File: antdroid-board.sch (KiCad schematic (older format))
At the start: 53 parts, among them Q1 BSS138, Q2 BSS138, U1 LM2678T-5.0, U2 LM2678T-5.0, U3 LM2675M-5

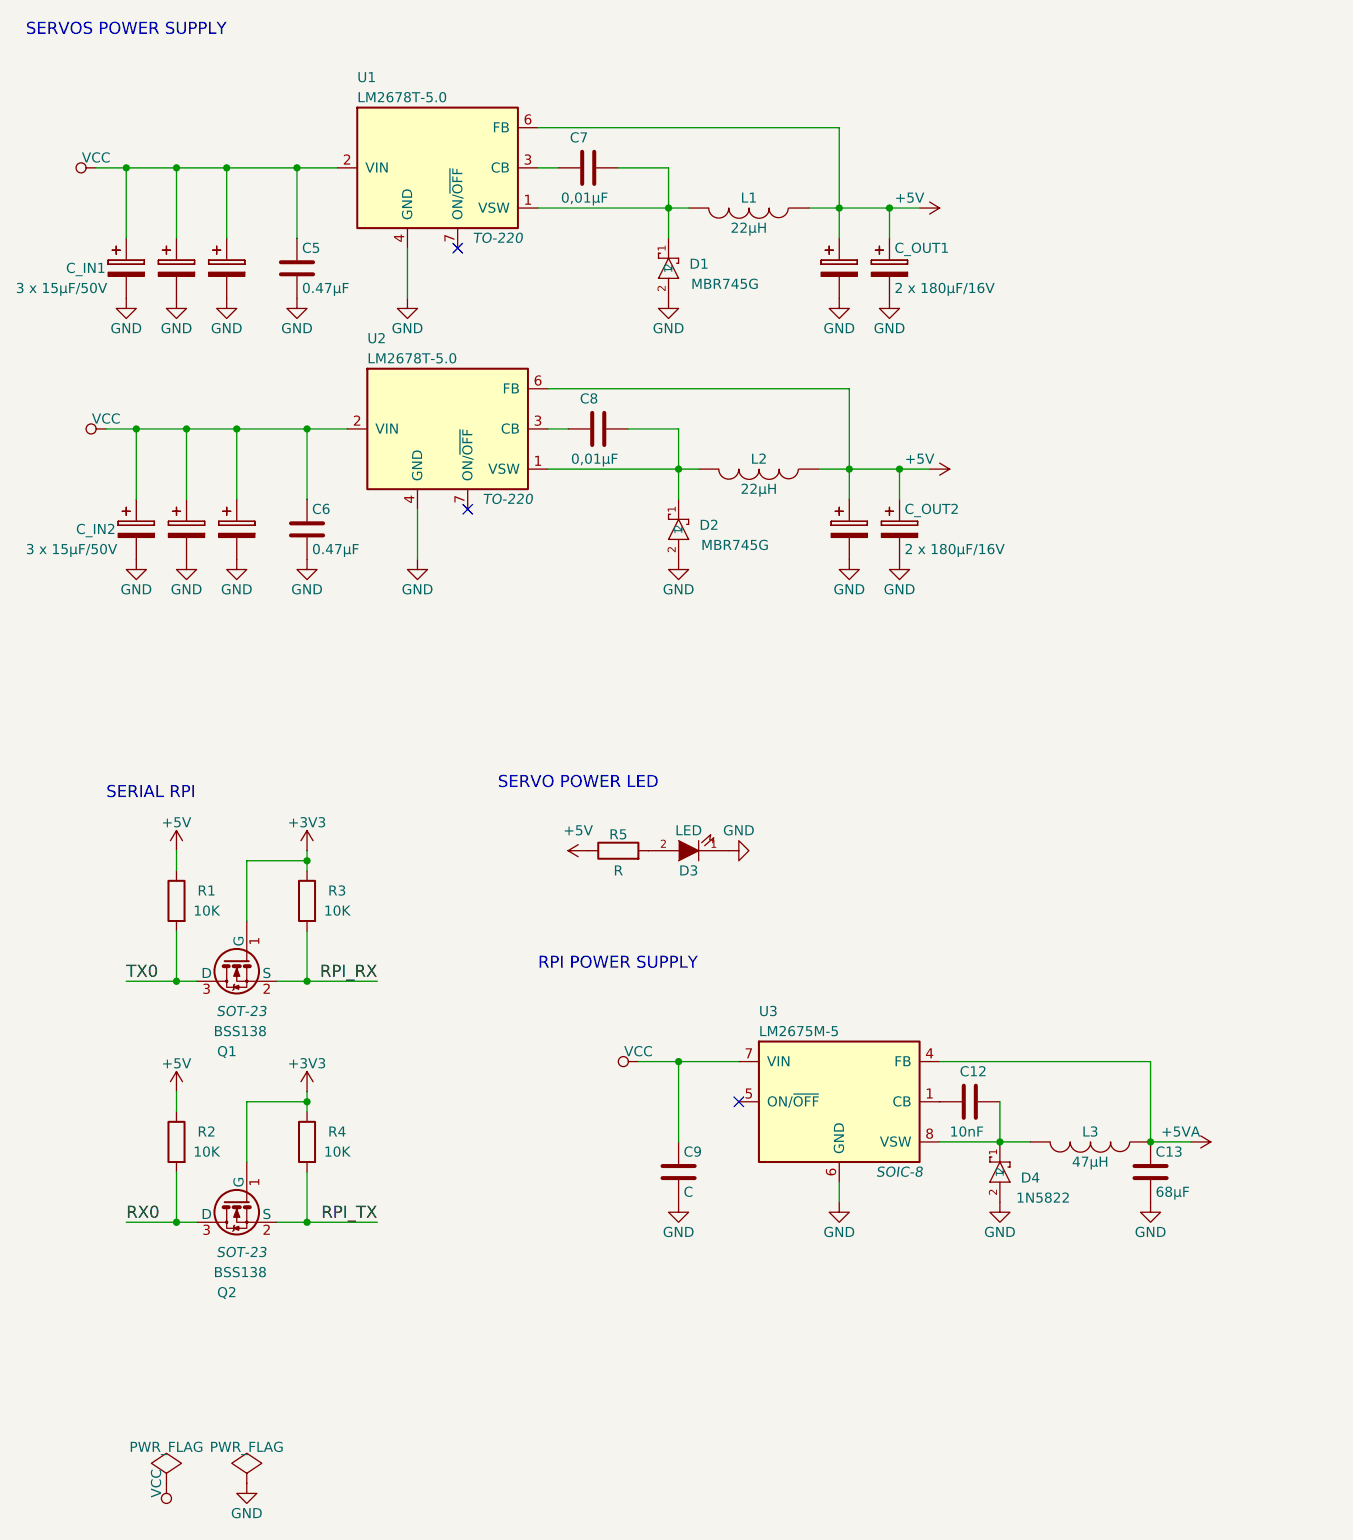
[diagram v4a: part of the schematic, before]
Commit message: PSU components fixed and some datasheet added
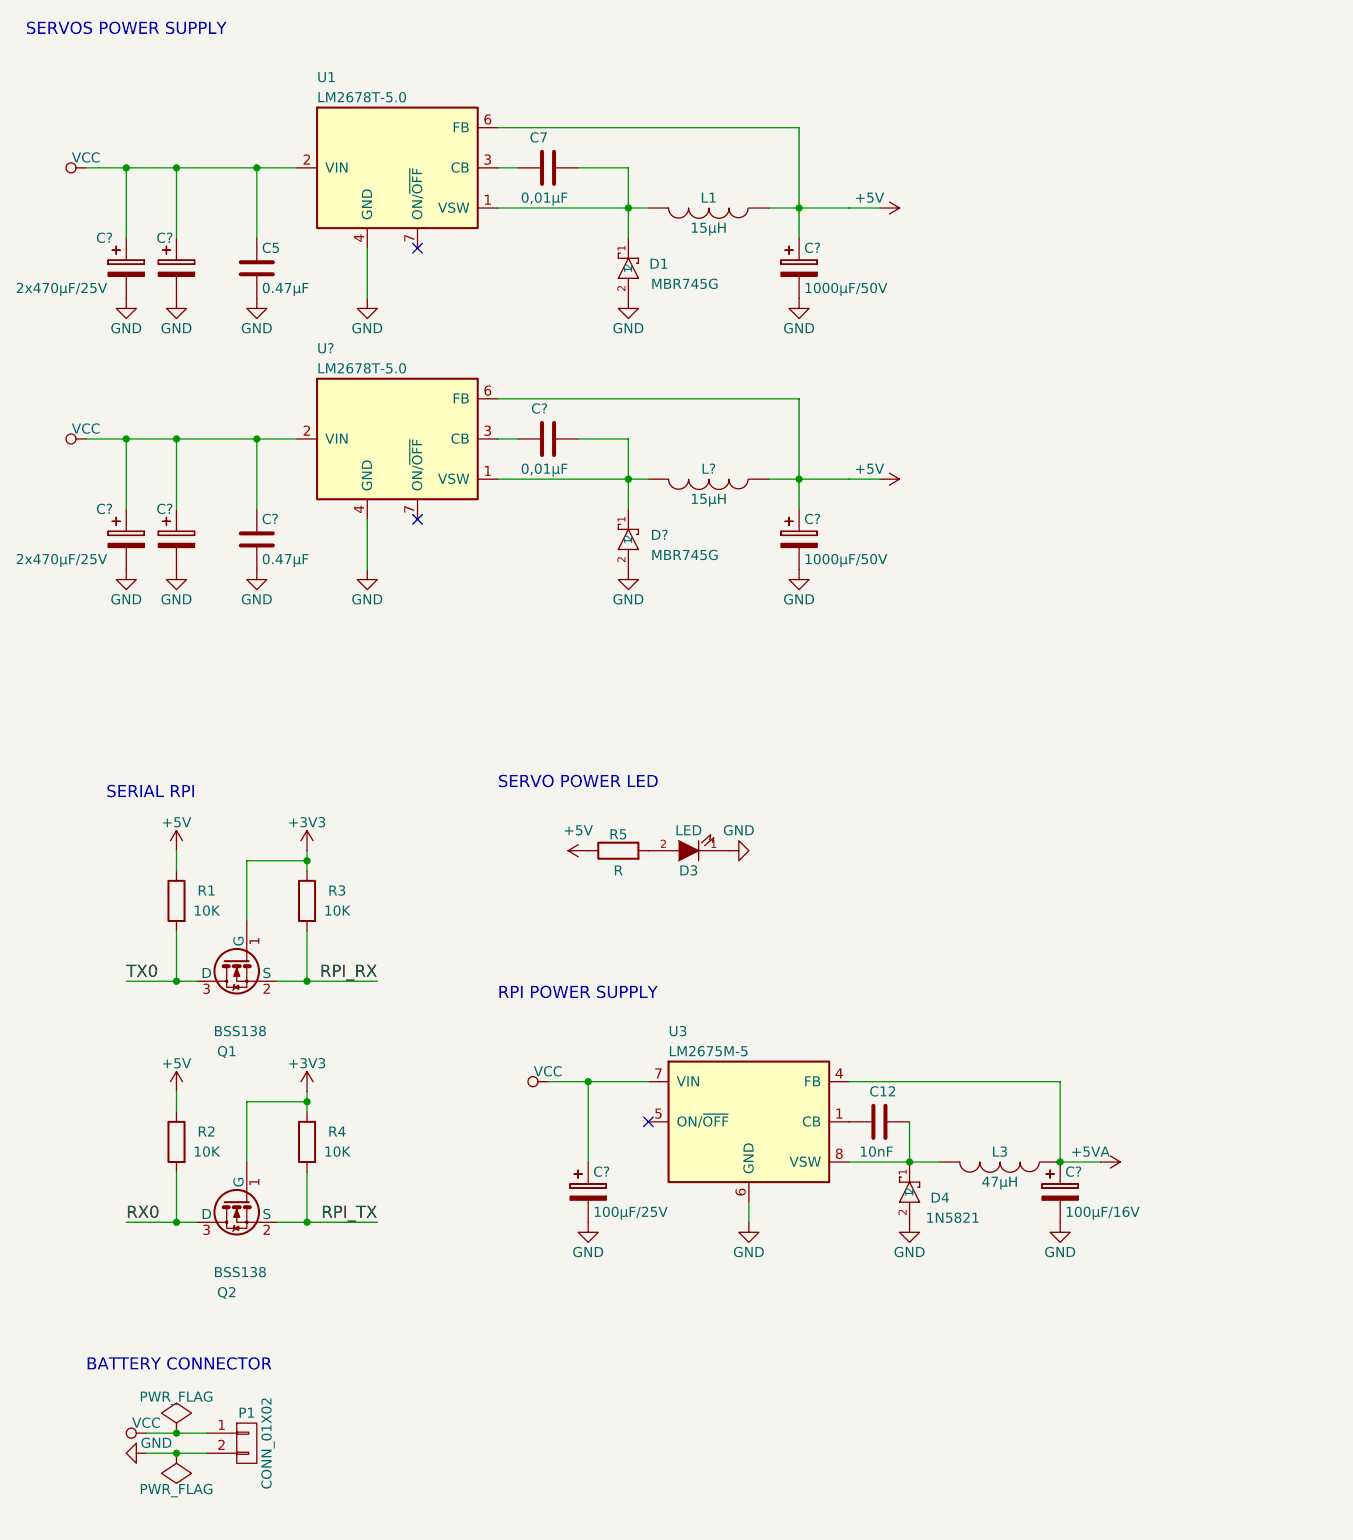
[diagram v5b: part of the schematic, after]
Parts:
- removed C1, C2, C3, C4: 15µF/50V, symbol CP
- removed C10, C11: 180µF/16V, symbol CP
- removed C13: 68µF, symbol C
- removed C6: 0.47µF, symbol C
- removed C8: 0,01µF, symbol C
- removed C9: C, symbol C
- removed C_IN2: 3 x 15µF/50V, symbol CP
- removed C_OUT2: 2 x 180µF/16V, symbol CP
- removed D2: MBR745G, DO-204AL, symbol MBR745G
- removed L2: 22µH, symbol INDUCTOR
- removed U2: LM2678T-5.0, TO-220, symbol LM2678T-5.0
- added C? (x2): 2x470µF/25V, symbol CP
- added C?: 470µF/25V, symbol CP
- added C?: 0.47µF, symbol C
- added C?: 0,01µF, symbol C
- added C?: 1000µF/50V, symbol CP
- added C?: 100µF/25V, symbol CP
- added C?: 100µF/16V, symbol CP
- added D?: MBR745G, DO-204AL, symbol MBR745G
- added L?: 15µH, LCI-50, symbol INDUCTOR
- added P1: CONN_01X02, symbol CONN_01X02
- added U?: LM2678T-5.0, Power_Integrations:TO-220, symbol LM2678T-5.0
- C?: renamed from C_IN1; value 3 x 15µF/50V -> 470µF/25V
- C?: renamed from C_OUT1; value 2 x 180µF/16V -> 1000µF/50V
- D4: value 1N5822 -> 1N5821
- JP1, JP10, JP11, JP12, JP13, JP14, JP15, JP16, JP17, JP18, JP2, JP3, JP4, JP5, JP6, JP7, JP8, JP9: footprint pinhead-1-1X03 -> Pin_Headers:Pin_Header_Straight_1x03
- L1: value 22µH -> 15µH; footprint (none) -> LCI-50
- Q1, Q2: footprint SOT-23 -> Housings_SOT-23_SOT-143_TSOT-6:SOT-23
- SHIELD1: footprint (none) -> arduino_shields:ARDUINO MEGA SHIELD
- U1: footprint TO-220 -> Power_Integrations:TO-220
- U3: footprint SOIC-8 -> ab2_so:AB2_SO08
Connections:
- net +5V: now also C?.1, L?.1, U?.6 (FB)
- net +5VA: now also C?.1
- net GND: now also C?.2, C?.2, C?.2, C?.2, C?.2, C?.2, C?.2, D?.2, P1.2 (P2), U?.4 (GND)
- net VCC: now also C?.1, C?.1, C?.1, C?.1, C?.1, P1.1 (P1), U?.2 (VIN)
- new net: C?.2, D?.1, L?.2, U?.1 (VSW)
- new net: C?.1, U?.3 (CB)
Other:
- note added: "BATTERY CONNECTOR"
- moved on the sheet: C12, C5, C7, C?, D1, D4, L1, L3, U1, U3

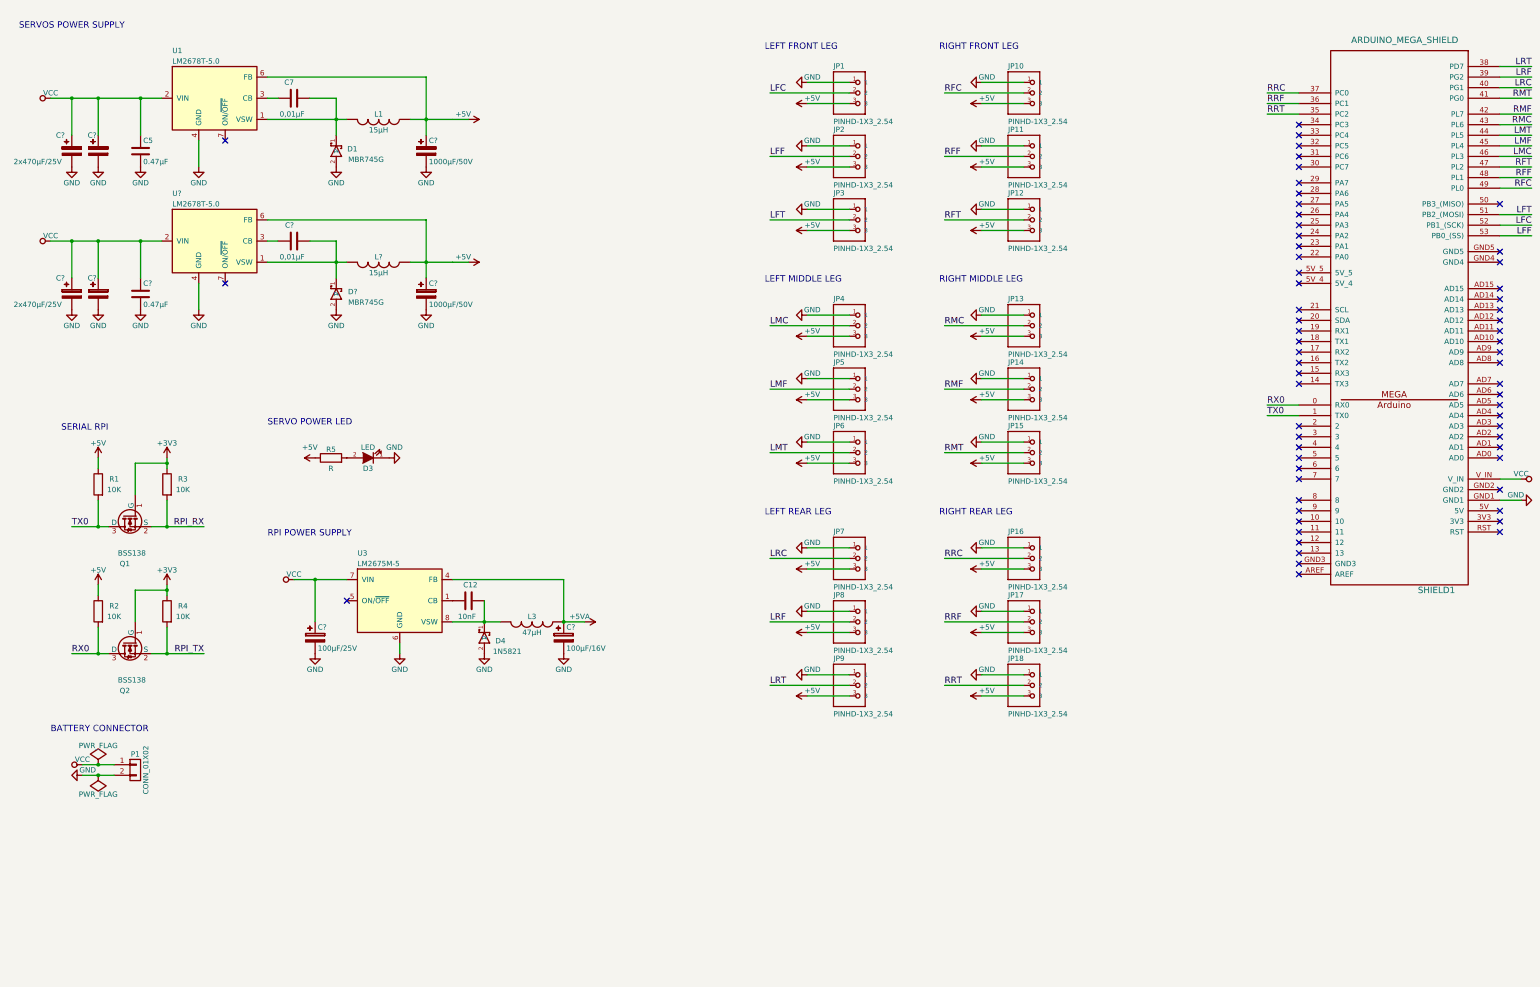
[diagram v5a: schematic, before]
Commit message: Change all 5V and 3V3 connections, resize papper
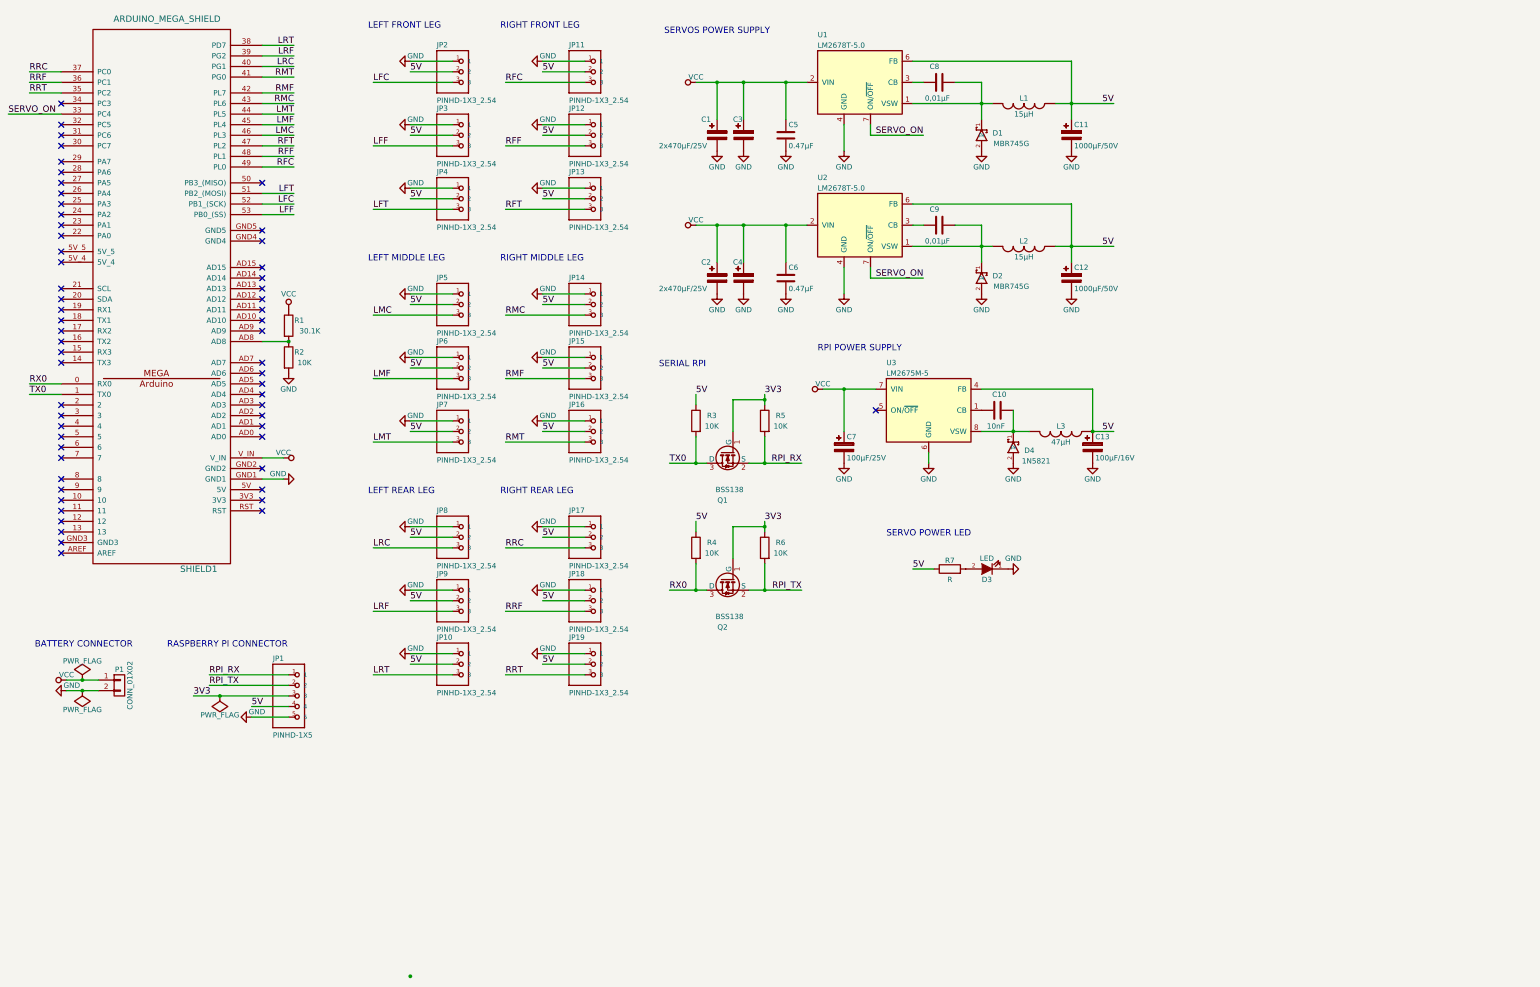
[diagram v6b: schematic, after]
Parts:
- added JP1: PINHD-1X5, pinhead-1X05, symbol PINHD-1X5
- added R1: 30.1K, symbol R
- added R2: 10K, symbol R
- gave numbers to parts that had none: 13
- renumbered C12 to C10, C7 to C8, JP9 to JP10, JP10 to JP11, JP11 to JP12, JP12 to JP13, JP13 to JP14, JP14 to JP15, JP15 to JP16, JP16 to JP17, JP17 to JP18, JP18 to JP19, JP1 to JP2, JP2 to JP3, JP3 to JP4, JP4 to JP5, JP5 to JP6, JP6 to JP7, JP7 to JP8, JP8 to JP9, R1 to R3, R2 to R4, R3 to R5, R4 to R6, R5 to R7
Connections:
- net GND: now also JP1.5, R2.2
- net LFC: now also JP2.3; no longer JP2.2
- net LFF: now also JP3.3; no longer JP3.2
- net LFT: now also JP4.3; no longer JP4.2
- net LMC: now also JP5.3; no longer JP5.2
- net LMF: now also JP6.3; no longer JP6.2
- net LMT: now also JP7.3; no longer JP7.2
- net LRC: now also JP8.3; no longer JP8.2
- net LRF: now also JP9.3; no longer JP9.2
- net LRT: now also JP10.3; no longer JP10.2
- net RFC: now also JP11.3; no longer JP11.2
- net RFF: now also JP12.3; no longer JP12.2
- net RFT: now also JP13.3; no longer JP13.2
- net RMC: now also JP14.3; no longer JP14.2
- net RMF: now also JP15.3; no longer JP15.2
- net RMT: now also JP16.3; no longer JP16.2
- net RPI_RX: now also JP1.1
- net RPI_TX: now also JP1.2
- net RRC: now also JP17.3; no longer JP17.2
- net RRF: now also JP18.3; no longer JP18.2
- net RRT: now also JP19.3; no longer JP19.2
- net VCC: now also R1.1
- net SERVO_ON: now reaches SHIELD1.33 (PC4)
- net SERVO_ON: now also U1.7 (ON/~OFF), U2.7 (ON/~OFF)
- net at SHIELD1.AD8: now also R1.2, R2.1
- net +3V3 renamed 3V3
- net 3V3: now also JP1.3
- removed net +5V: C11.1, C12.1, JP10.3, JP11.3, JP12.3, JP13.3, JP14.3, JP15.3, JP16.3, JP17.3, JP18.3, JP19.3, JP2.3, JP3.3, JP4.3, JP5.3, JP6.3, JP7.3, JP8.3, JP9.3, L1.1, L2.1, R3.1, R4.1, R7.1, U1.6 (FB), U2.6 (FB)
- net +5VA renamed 5V
- net 5V: now also C11.1, C12.1, JP10.2, JP11.2, JP12.2, JP13.2, JP14.2, JP15.2, JP16.2, JP17.2, JP18.2, JP19.2, JP2.2, JP3.2, JP4.2, JP5.2, JP6.2, JP7.2, JP8.2, JP9.2, L1.1, L2.1, R3.1, R4.1, R7.1, U1.6 (FB), U2.6 (FB), JP1.4
- no-connect marks 63 -> 59
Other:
- note added: "RASPBERRY PI CONNECTOR"
- moved on the sheet: C1, C10, C11, C12, C13, C2, C3, C4, C5, C6, C7, C8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
